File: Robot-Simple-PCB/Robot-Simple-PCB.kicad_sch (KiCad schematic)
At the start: 71 parts, among them J1 Main Power In, J10 PiicoDev, J11 MotA, J12 MotB, J13 Mot3, J14 Ext_PWR_Sw, J2 Servo1, J3 Servo1, J4 Servo2, J5 Servo2, J6 Servo3, J7 Servo4, J8 Plug and pair, J9 UART_Conn, Q1 Q_PMOS_DGS, Q2 Q_PMOS_DGS, SW1 Onboard_PWR_Sw, SW2 SW_Push, U1 ESP32-S3-WROOM-1, U2 DRV8871DDA, U3 DRV8871DDA, U4 DRV8871DDA, U5 AMS1117-3.3, U6 TPS54302

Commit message: More workin
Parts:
- removed D1: WS2812B, LED_SMD:LED_WS2812B_PLCC4_5.0x5.0mm_P3.2mm, symbol LED:WS2812B
- removed D8, D9: RED_LED, symbol Device:LED
- removed J9: UART_Conn, symbol Connector:Conn_01x03_Socket
- removed Q1, Q2: Q_PMOS_DGS, symbol Device:Q_PMOS_DGS
- removed U1: ESP32-S3-WROOM-1, RF_Module:ESP32-S3-WROOM-1, symbol RF_Module:ESP32-S3-WROOM-1
- added C8: 1u, Capacitor_SMD:C_0402_1005Metric, symbol Device:C
- added D1: D_Schottky, Diode_SMD:D_SOD-123, symbol Device:D_Schottky
- added D11: ORANGE_LED, LED_SMD:LED_0603_1608Metric, symbol Device:LED
- added D12: WS2812B, LED_SMD:LED_WS2812B_PLCC4_5.0x5.0mm_P3.2mm, symbol LED:WS2812B
- added J15: PSU_in, Connector_PinHeader_2.54mm:PinHeader_1x02_P2.54mm_Vertical, symbol Connector:Conn_01x02_Socket
- added J16: PSU_out, Connector_PinHeader_2.54mm:PinHeader_1x02_P2.54mm_Vertical, symbol Connector:Conn_01x02_Socket
- added J17: WS2812_Out, Connector_PinHeader_2.54mm:PinHeader_1x03_P2.54mm_Vertical, symbol Connector:Conn_01x03_Socket
- added J18: Prog_Header, Connector_PinHeader_2.54mm:PinHeader_1x06_P2.54mm_Vertical, symbol Connector:Conn_01x06_Socket
- added J19: Breakout_Header, Connector_PinHeader_2.54mm:PinHeader_1x14_P2.54mm_Vertical, symbol Connector:Conn_01x14_Socket
- added J20: UART_Conn, Connector_PinHeader_2.54mm:PinHeader_1x04_P2.54mm_Vertical, symbol Connector:Conn_01x04_Pin
- added JP1: PSU_out, Jumper:SolderJumper-2_P1.3mm_Open_RoundedPad1.0x1.5mm, symbol Jumper:Jumper_2_Open
- added JP2: PSU_in, Jumper:SolderJumper-2_P1.3mm_Open_RoundedPad1.0x1.5mm, symbol Jumper:Jumper_2_Open
- added JP3: Rev_Volt_out, Jumper:SolderJumper-2_P1.3mm_Open_RoundedPad1.0x1.5mm, symbol Jumper:Jumper_2_Open
- added JP4: Rev_Volt_in, Jumper:SolderJumper-2_P1.3mm_Open_RoundedPad1.0x1.5mm, symbol Jumper:Jumper_2_Open
- added Q3, Q4: Q_PMOS_GDS, Package_TO_SOT_SMD:TO-252-2, symbol Device:Q_PMOS_GDS
- added R20: 10k, Resistor_SMD:R_0402_1005Metric_Pad0.72x0.64mm_HandSolder, symbol Device:R
- added R21, R22: R, Resistor_SMD:R_0402_1005Metric_Pad0.72x0.64mm_HandSolder, symbol Device:R
- added R23, R24, R25, R26: 100, Resistor_SMD:R_0402_1005Metric_Pad0.72x0.64mm_HandSolder, symbol Device:R
- added TP6: Vf_TP, TestPoint:TestPoint_THTPad_D1.0mm_Drill0.5mm, symbol Connector:TestPoint
- added U1, U8: 74LVC2G34GW, Package_TO_SOT_SMD:SOT-23-6, symbol Liam_Generic_symbols:74LVC2G34GW
- added U7: ESP32-S3-WROOM-1, RF_Module:ESP32-S3-WROOM-1, symbol RF_Module:ESP32-S3-WROOM-1
- C1, C2, C5, C6: footprint (none) -> Capacitor_SMD:C_0402_1005Metric; MPN (none) -> C1523
- C3, C4: footprint (none) -> Capacitor_SMD:C_0402_1005Metric; MPN (none) -> C1581
- C7: footprint (none) -> Capacitor_SMD:C_0402_1005Metric; MPN (none) -> C1546
- D10, D4, D5, D6, D7: footprint (none) -> LED_SMD:LED_0603_1608Metric
- D2, D3: MPN (none) -> C5349953
- H1, H2, H3, H4: footprint (none) -> MountingHole:MountingHole_4.3mm_M4
- J1, J11, J12, J13: footprint (none) -> Connector_Phoenix_MC:PhoenixContact_MCV_1,5_2-G-3.5_1x02_P3.50mm_Vertical
- J10: footprint (none) -> Connector_JST:JST_SH_SM04B-SRSS-TB_1x04-1MP_P1.00mm_Horizontal
- J14: footprint (none) -> Connector_PinHeader_2.54mm:PinHeader_1x02_P2.54mm_Vertical
- J2, J3, J4, J5, J6, J7: footprint (none) -> Connector_PinHeader_2.54mm:PinHeader_1x03_P2.54mm_Vertical
- J8: footprint (none) -> Connector_PinSocket_2.54mm:PinSocket_1x05_P2.54mm_Vertical
- L1: value 10u -> 10uL; footprint (none) -> Inductor_SMD:L_Chilisin_BMRB00060612; MPN (none) -> C128692
- R1, R11, R12, R15, R16, R17, R18, R19, R2, R3, R7, R9: footprint (none) -> Resistor_SMD:R_0402_1005Metric_Pad0.72x0.64mm_HandSolder
- R10, R4, R8: footprint (none) -> Resistor_THT:R_Axial_DIN0207_L6.3mm_D2.5mm_P10.16mm_Horizontal
- R13, R5, R6: footprint Resistor_SMD:R_1206_3216Metric -> Resistor_SMD:R_0402_1005Metric_Pad0.72x0.64mm_HandSolder
- R14: value R -> 10k; footprint Resistor_SMD:R_1206_3216Metric -> Resistor_SMD:R_0402_1005Metric_Pad0.72x0.64mm_HandSolder
- SW1: footprint (none) -> Button_Switch_SMD:SW_SPDT_PCM12; MPN (none) -> C431541
- SW2: value SW_Push -> User_Button; footprint (none) -> Button_Switch_SMD:SW_Push_1P1T_NO_6x6mm_H9.5mm; MPN (none) -> C7470157
- TP1, TP2, TP3, TP4, TP5: footprint (none) -> TestPoint:TestPoint_THTPad_D1.0mm_Drill0.5mm
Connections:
- net +3.3V: now also J20.4 (Pin_4)
- net +3V3: now also J18.1 (Pin_1), J19.2 (Pin_2), J19.3 (Pin_3), R20.1, R21.1, U7.2 (3V3)
- net +5V: now also D1.2 (A), J19.1 (Pin_1); no longer C5.1, C6.1, J2.2 (Pin_2), J3.2 (Pin_2), J4.2 (Pin_2), J5.2 (Pin_2), J6.2 (Pin_2), J7.2 (Pin_2), L1.2, R17.1, TP5.1, U5.3 (VI)
- net GND: now also D2.3 (VSS), D3.3 (VSS), D5.1 (K), SW2.2, C8.2, D11.1 (K), D12.3 (VSS), J15.1 (Pin_1), J16.1 (Pin_1), J17.3 (Pin_3), J18.6 (Pin_6), J19.13 (Pin_13), J19.14 (Pin_14), J19.8 (Pin_8), J20.1 (Pin_1), U1.2 (GND), U7.1 (GND), U7.40 (GND), U7.41 (GND), U8.2 (GND)
- net I2C0_SCL: now also U7.7 (IO7)
- net I2C0_SDA: now also U7.6 (IO6)
- net Mot1_A: now also U7.31 (IO38)
- net Mot1_B: now also U7.32 (IO39)
- net Mot2_A: now also U7.33 (IO40)
- net Mot2_B: now also U7.34 (IO41)
- net Mot3_A: now also U7.24 (IO47)
- net Mot3_B: now also U7.25 (IO48)
- net PAIR_LED: now also R13.1, U7.18 (IO10)
- net Servo_Sig_1: now also U1.1 (1A), U7.39 (IO1); no longer J2.3 (Pin_3), J3.3 (Pin_3)
- net Servo_Sig_2: now also U1.3 (2A), U7.38 (IO2); no longer J4.3 (Pin_3), J5.3 (Pin_3)
- net Servo_Sig_3: now also U7.4 (IO4), U8.1 (1A); no longer J6.3 (Pin_3)
- net Servo_Sig_4: now also U7.5 (IO5), U8.3 (2A); no longer J7.3 (Pin_3)
- net UART0_RXD: now also U7.12 (IO8)
- net UART0_TXD: now also U7.17 (IO9)
- net VBAT: now also J15.2 (Pin_2), JP2.1 (A), JP3.2 (B); no longer C2.1, C3.1, R15.1, R5.1, TP3.1, U6.3 (VIN)
- net USER_BUTTON: now reaches SW2.1
- net USER_BUTTON: now also J19.10 (Pin_10), U7.35 (IO42)
- net at D2.1 (VDD): now also D1.1 (K)
- net at D2.2 (DOUT): now also D3.4 (DIN)
- net USER_WS2812: now reaches D2.4 (DIN)
- net USER_WS2812: now also U7.11 (IO18)
- net +5VP: now reaches D3.1 (VDD)
- net +5VP: now also C5.1, C6.1, J2.2 (Pin_2), J3.2 (Pin_2), J4.2 (Pin_2), J5.2 (Pin_2), J6.2 (Pin_2), J7.2 (Pin_2), L1.2, R17.1, TP5.1, D12.1 (VDD), J17.1 (Pin_1), JP1.1 (A), U1.5 (Vcc), U8.5 (Vcc)
- net at D3.2 (DOUT): now also D12.4 (DIN)
- net at D7.2 (A): now also R21.2; no longer R14.2
- net at R13.2: now also D5.2 (A)
- net at F2.2: now also JP4.1 (A), TP6.1
- net at D6.2 (A), R12.1: now also Q3.1 (G), Q4.1 (G)
- net at D6.1 (K), R11.1: now also Q3.3 (S), Q4.3 (S)
- new net: JP3.1 (A), Q4.2 (D), R5.1, TP3.1
- new net: J7.3 (Pin_3), R26.2
- new net: R24.1, U1.4 (2Y)
- new net: R23.1, U1.6 (1Y)
- new net: D11.2 (A), R22.2
- new net: J16.2 (Pin_2), U5.3 (VI)
- new net: J4.3 (Pin_3), J5.3 (Pin_3), R24.2
- new net: J2.3 (Pin_3), J3.3 (Pin_3), R23.2
- new net: J6.3 (Pin_3), R25.2
- new net: C2.1, C3.1, JP2.2 (B), R15.1, U6.3 (VIN)
- new net: R25.1, U8.6 (1Y)
- new net: R26.1, U8.4 (2Y)
- new net: D12.2 (DOUT), J17.2 (Pin_2)
- new net: JP4.2 (B), Q3.2 (D)
- new net BKT_IO13: J19.4 (Pin_4), U7.21 (IO13)
- new net BKT_IO14: J19.5 (Pin_5), U7.22 (IO14)
- new net BKT_IO15: J19.6 (Pin_6), U7.8 (IO15)
- new net BKT_IO16: J19.7 (Pin_7), U7.9 (IO16)
- new net BKT_IO21: J19.9 (Pin_9), U7.23 (IO21)
- new net BOOT: J18.2 (Pin_2), R14.2, U7.27 (IO0)
- new net EN: C8.1, J18.3 (Pin_3), R20.2, U7.3 (EN)
- new net HB_LED: R22.1, U7.10 (IO17)
- new net RX_D: J18.5 (Pin_5), U7.36 (RXD0)
- new net TX_D: J18.4 (Pin_4), U7.37 (TXD0)
- new net UART1_RXD: J20.3 (Pin_3), U7.19 (IO11)
- new net UART1_TXD: J20.2 (Pin_2), U7.20 (IO12)
- new net USB_D+: U7.14 (IO20)
- new net USB_D-: U7.13 (IO19)
- no-connect marks 0 -> 8
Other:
- note added: "(800mA rated stall, testing ~500mA)"
- note added: "(BKT_IO42)"
- note added: "Around 10A through here"
- note added: "BKT = Breakout"
- note added: "ESP32-S3(16MB): C2913205"
- note added: "EXPANSION MODULE IDEAS: MALCOLM REQUEST Some protected analog inputs? With 5 or 3.3v supply and ground pins next to them"
- note added: "If another MCU wants to turn this on and off Use a SSR, or analog switch to short these"
- note added: "LLC - C7394039"
- note added: "PFET - C41355208"
- note added: "Power pref here"
- note added: "Red LEDs for power Orange for Heartbeats"
- note added: "TODO USB connector Split 5V and 5VP (5V should just power the ESP32(3.3V stuff), no motors etc ERC"
- note removed: "At least 4 sets, have it so that 2 sets have 2 connector outputs LLC for each"
- note removed: "If another MCU wants to turn this on and off Use a SSR, or analog switch"
- note removed: "MCU Power"
- note removed: "Red LEDs for power"
- moved on the sheet: C1, C2, C3, C4, C5, C6, C7, D4, D6, F2, J11, J12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

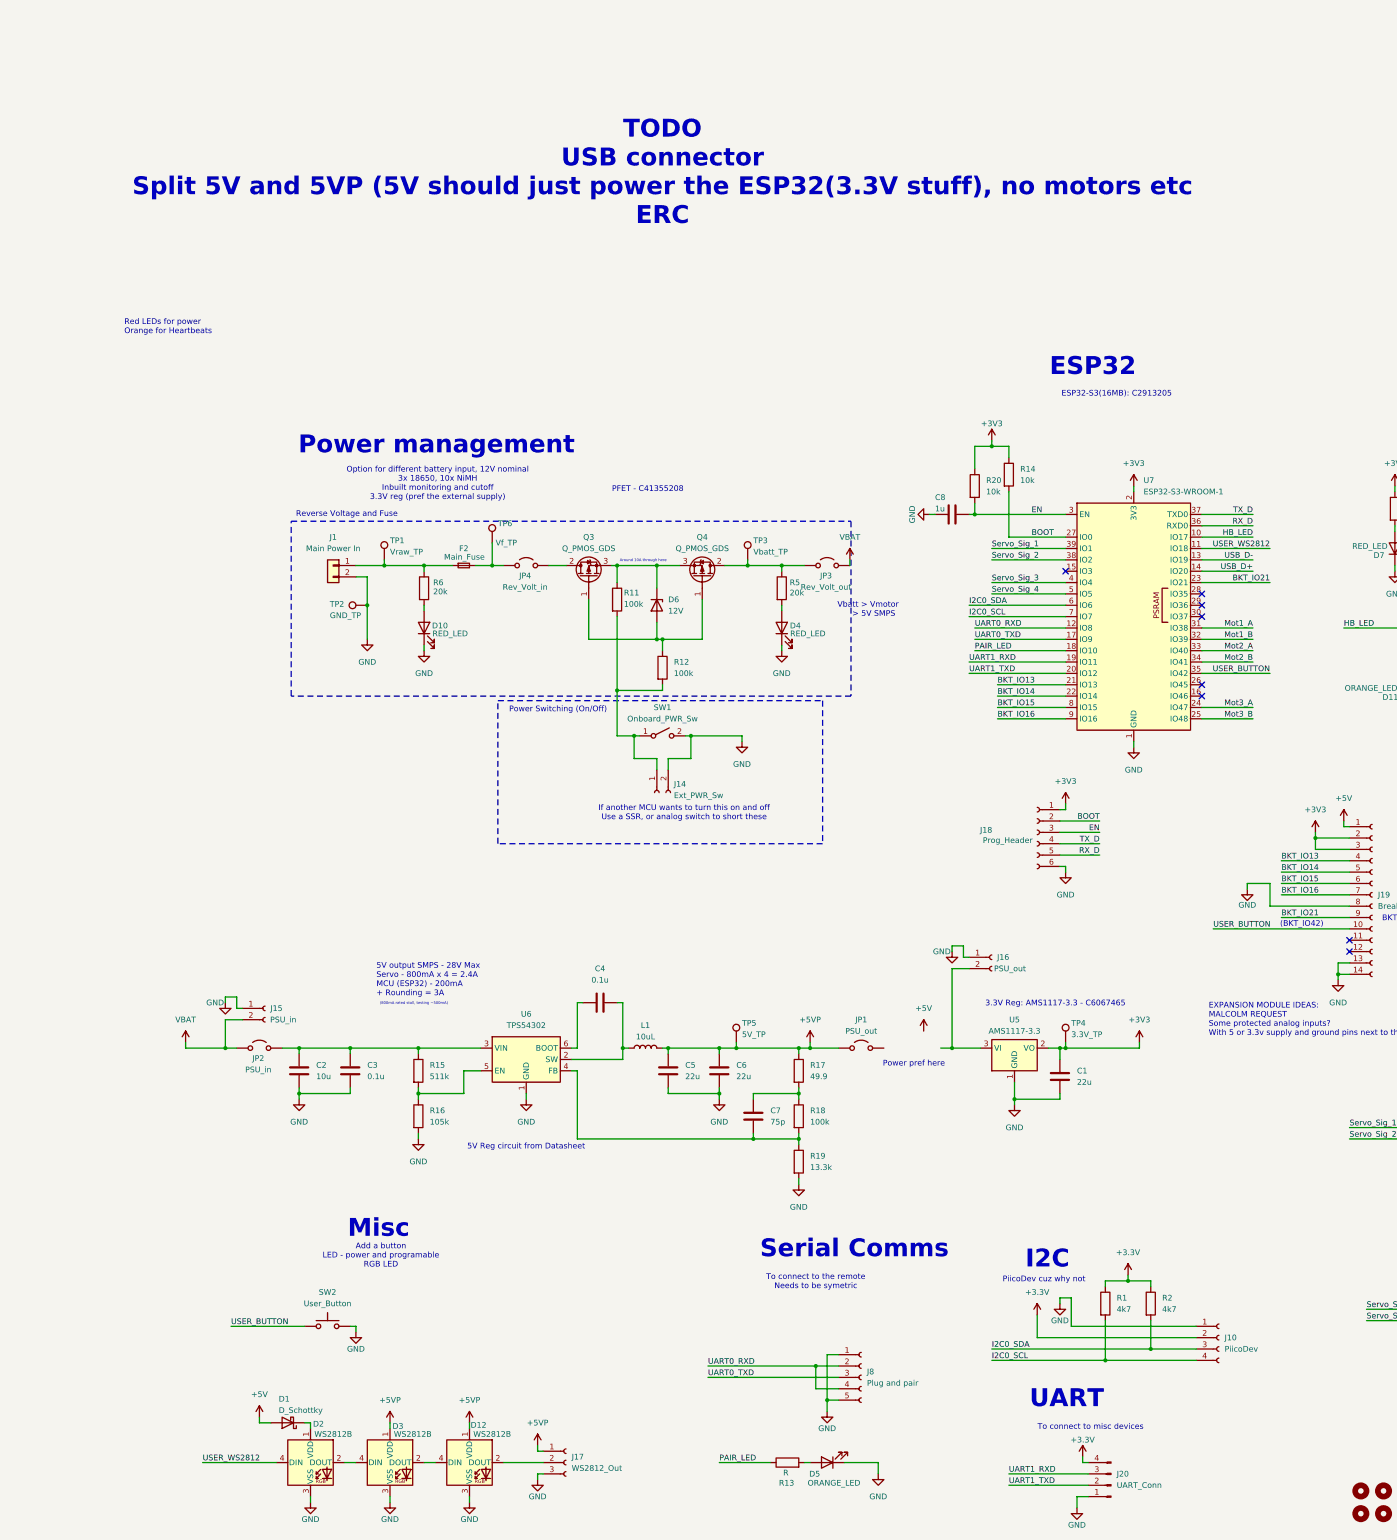
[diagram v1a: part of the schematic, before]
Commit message: Schematic complete, started routing
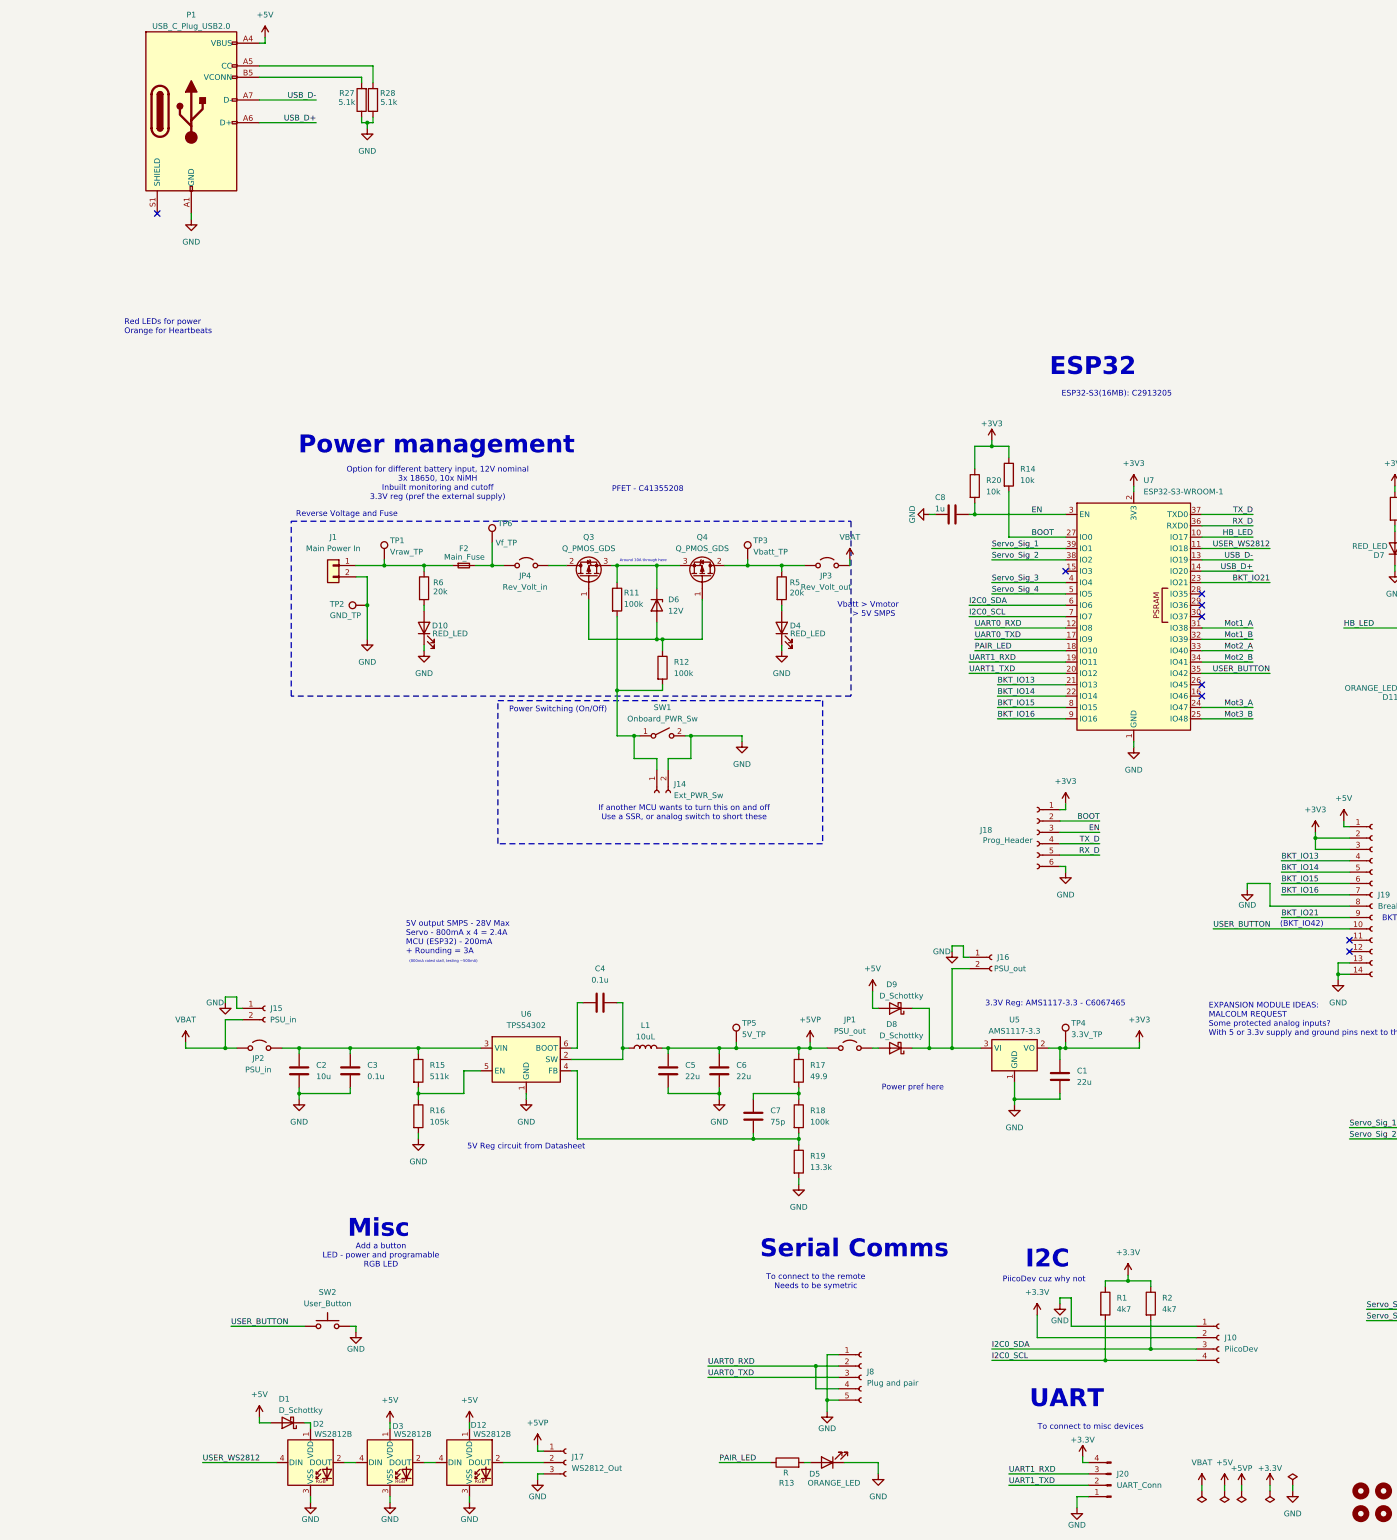
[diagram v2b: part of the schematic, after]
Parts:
- added D8, D9: D_Schottky, Diode_SMD:D_SOD-123, symbol Device:D_Schottky
- added P1: USB_C_Plug_USB2.0, Connector_USB:USB_C_Receptacle_GCT_USB4125-xx-x_6P_TopMnt_Horizontal, symbol Connector:USB_C_Plug_USB2.0
- added R27, R28: 5.1k, Resistor_SMD:R_0402_1005Metric_Pad0.72x0.64mm_HandSolder, symbol Device:R
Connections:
- net +5V: now also D12.1 (VDD), D3.1 (VDD), D9.2 (A), P1.A4 (VBUS), P1.A9 (VBUS), P1.B4 (VBUS), P1.B9 (VBUS)
- net +5VP: no longer D12.1 (VDD), D3.1 (VDD)
- net GND: now also P1.A1 (GND), P1.A12 (GND), P1.B1 (GND), P1.B12 (GND), R27.1, R28.1
- net USB_D+: now also P1.A6 (D+)
- net USB_D-: now also P1.A7 (D-)
- net at JP1.2 (B): now also D8.2 (A)
- net at J16.2 (Pin_2), U5.3 (VI): now also D8.1 (K), D9.1 (K)
- new net: P1.B5 (VCONN), R27.2
- new net: P1.A5 (CC), R28.2
- no-connect marks 8 -> 9
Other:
- note removed: "TODO USB connector Split 5V and 5VP (5V should just power the ESP32(3.3V stuff), no motors etc ERC"
- moved on the sheet: JP1

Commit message: Yuuuuh
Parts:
- removed JP3: Rev_Volt_out, Jumper:SolderJumper-2_P1.3mm_Open_RoundedPad1.0x1.5mm, symbol Jumper:Jumper_2_Open
- removed P1: USB_C_Plug_USB2.0, Connector_USB:USB_C_Receptacle_GCT_USB4125-xx-x_6P_TopMnt_Horizontal, symbol Connector:USB_C_Plug_USB2.0
- added C9: 10u, Capacitor_SMD:C_1206_3216Metric, symbol Device:C
- added J9: USB_C_Receptacle_USB2.0_16P, Connector_USB:USB_C_Receptacle_HCTL_HC-TYPE-C-16P-01A, symbol Connector:USB_C_Receptacle_USB2.0_16P
- C1, C5, C6: footprint Capacitor_SMD:C_0402_1005Metric -> Capacitor_SMD:C_1206_3216Metric
- C2: footprint Capacitor_SMD:C_0402_1005Metric -> Capacitor_SMD:C_1206_3216Metric; MPN C1523 -> C13585
- C3, C4: footprint Capacitor_SMD:C_0402_1005Metric -> Capacitor_SMD:C_0603_1608Metric; MPN C1581 -> C14663
- R21, R22: value R -> 10k
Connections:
- net +3.3V is gone; now on net +3V3: J10.2 (Pin_2), J20.4 (Pin_4), R1.1, R2.1
- net +5V: now also D8.1 (K), D9.1 (K), J16.2 (Pin_2), U5.3 (VI); no longer D9.2 (A)
- net +5VP: now also D8.2 (A), JP1.2 (B); no longer C5.1, C6.1, JP1.1 (A), L1.2, R17.1, TP5.1
- net GND: now also C9.2, J9.A1 (GND), J9.A12 (GND), J9.B1 (GND), J9.B12 (GND)
- net HB_LED: now also U7.11 (IO18); no longer U7.10 (IO17)
- net I2C0_SCL: now also U7.9 (IO16); no longer U7.7 (IO7)
- net I2C0_SDA: now also U7.8 (IO15); no longer U7.6 (IO6)
- net Mot1_A: now also U7.23 (IO21); no longer U7.31 (IO38)
- net Mot1_B: now also U7.24 (IO47); no longer U7.32 (IO39)
- net Mot2_A: now also U7.21 (IO13); no longer U7.33 (IO40)
- net Mot2_B: now also U7.22 (IO14); no longer U7.34 (IO41)
- net Mot3_A: now also U7.19 (IO11); no longer U7.24 (IO47)
- net Mot3_B: now also U7.20 (IO12); no longer U7.25 (IO48)
- net PAIR_LED: now also U7.6 (IO6); no longer U7.18 (IO10)
- net Servo_Sig_1: now also U7.18 (IO10); no longer U7.39 (IO1)
- net Servo_Sig_2: now also U7.17 (IO9); no longer U7.38 (IO2)
- net Servo_Sig_3: now also U7.12 (IO8); no longer U7.4 (IO4)
- net Servo_Sig_4: now also U7.10 (IO17); no longer U7.5 (IO5)
- net UART0_RXD: now also U7.4 (IO4); no longer U7.12 (IO8)
- net UART0_TXD: now also U7.5 (IO5); no longer U7.17 (IO9)
- net UART1_RXD: now also U7.31 (IO38); no longer U7.19 (IO11)
- net UART1_TXD: now also U7.25 (IO48); no longer U7.20 (IO12)
- net USB_D+: now also J9.A6 (D+), J9.B6 (D+)
- net USB_D-: now also J9.A7 (D-), J9.B7 (D-)
- net USER_BUTTON: now also U7.7 (IO7); no longer U7.35 (IO42)
- net USER_WS2812: now also U7.32 (IO39); no longer U7.11 (IO18)
- net VBAT: now also Q4.2 (D), R5.1, TP3.1; no longer J15.2 (Pin_2)
- net at U4.6 (OUT1): now also J11.2 (Pin_2); no longer J11.1 (Pin_1)
- net at U4.8 (OUT2): now also J11.1 (Pin_1); no longer J11.2 (Pin_2)
- net at J13.1 (Pin_1): now also U2.8 (OUT2); no longer U2.6 (OUT1)
- net at J13.2 (Pin_2): now also U2.6 (OUT1); no longer U2.8 (OUT2)
- net at C2.1, C3.1, JP2.2 (B)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: now also J15.2 (Pin_2), C9.1
- net at U3.6 (OUT1): now also J12.2 (Pin_2); no longer J12.1 (Pin_1)
- net at U3.8 (OUT2): now also J12.1 (Pin_1); no longer J12.2 (Pin_2)
- net at R27.2: now also J9.B5 (CC2)
- net at R28.2: now also J9.A5 (CC1)
- net BKT_IO13 renamed BKT_IO40
- net BKT_IO40: now also U7.33 (IO40); no longer U7.21 (IO13)
- net BKT_IO14 renamed BKT_IO41
- net BKT_IO41: now also U7.34 (IO41); no longer U7.22 (IO14)
- net BKT_IO15 renamed BKT_IO42
- net BKT_IO42: now also U7.35 (IO42); no longer U7.8 (IO15)
- net BKT_IO16 renamed BKT_IO2
- net BKT_IO2: now also U7.38 (IO2); no longer U7.9 (IO16)
- net BKT_IO21 renamed BKT_IO1
- net BKT_IO1: now also U7.39 (IO1); no longer U7.23 (IO21)
- new net: C5.1, C6.1, JP1.1 (A), L1.2, R17.1, TP5.1
- new net VBUS: D9.2 (A), J9.A4 (VBUS), J9.A9 (VBUS), J9.B4 (VBUS), J9.B9 (VBUS)
- no-connect marks 9 -> 11
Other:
- note added: "(BKT_IO40)"
- note removed: "(BKT_IO42)"
- moved on the sheet: C2, C3, J15, JP1, JP2
